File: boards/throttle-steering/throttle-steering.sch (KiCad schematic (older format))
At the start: 58 parts, among them IC1 ATMEGA16M1, P1 CONN_02X03, Q1 SSM3K333R, Q2 SSM3K333R, Q3 SSM3K333R, U1 MCP6021T-E/OT, U2 CAN_Transceiver, U3 MCP6021T-E/OT, U4 TPS561201, Y1 Crystal_SMD

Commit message: Updated the steering-throttle schematic. Need to check footprints and create netlist before going to layout.
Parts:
- removed R10, R16, R5: R_499, Resistors_SMD:R_0805, symbol R_499
- removed R13, R4: R_10k, Resistors_SMD:R_0805, symbol R_10k
- removed R14: R_200, Resistors_SMD:R_0805, symbol R_200
- removed R15, R8: R_100, Resistors_SMD:R_0805, symbol R_100
- removed R7: R, symbol R
- removed U1, U3: MCP6021T-E/OT, symbol MCP6021T-E/OT
- added D7: D_Zener_18V, footprints:DO-214AA, symbol D_Zener_18V
- added R10, R15, R16, R5, R7: R_1k, footprints:R_0805_OEM, symbol R_1k
- added R13, R4: R_1M, footprints:R_0805_OEM, symbol R_1M
- added R14, R8: R_2.2k, footprints:R_0805_OEM, symbol R_2.2k
- added U1, U3: MCP6001RT, footprints:SOT-23-5_OEM, symbol MCP6001RT
- gave numbers to parts that had none: 2
- renumbered D7 to D8, R23 to R22, R24 to R23, R27 to R24, R28 to R27, R29 to R28
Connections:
- wire segments 97 -> 79
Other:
- note removed: "50\n"
- moved on the sheet: J2

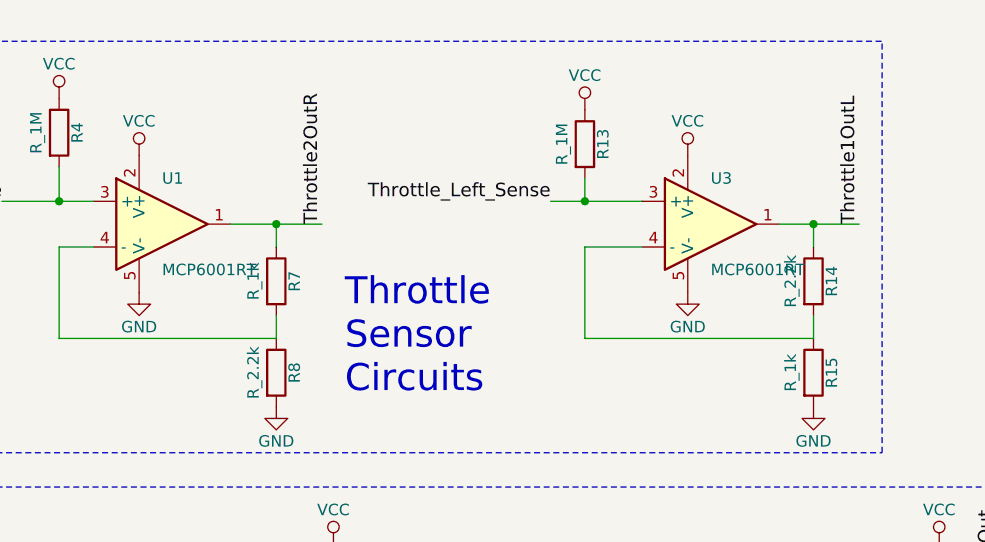
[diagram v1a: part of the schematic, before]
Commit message: Updated the throttle-steeting folder. Updated all of the footprints for the preset and began rough layout for board.
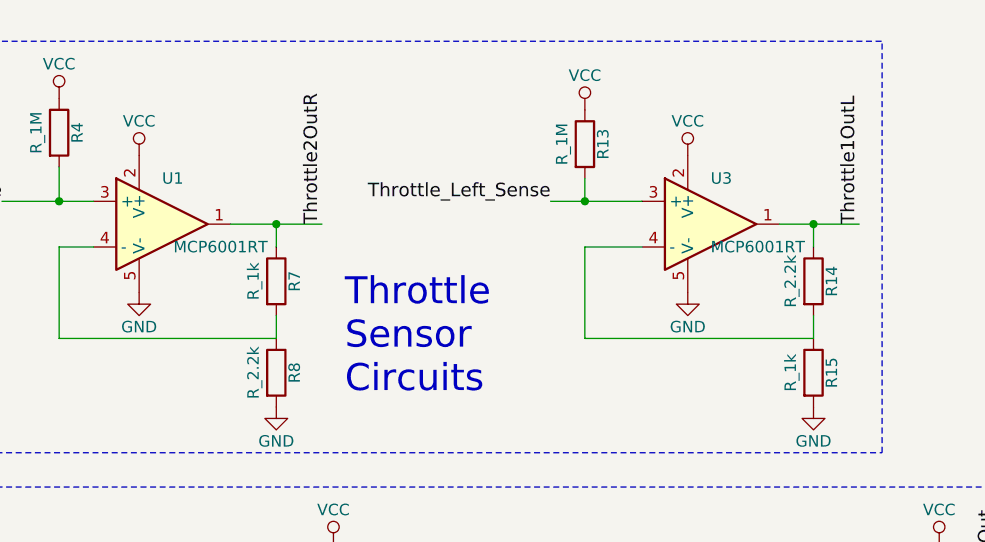
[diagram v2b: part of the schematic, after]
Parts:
- C1, C2, C3, C5, C6, C7, C8: footprint Capacitors_SMD:C_0805 -> footprints:C_0805_OEM
- C4: footprint Capacitors_SMD:C_1206 -> footprints:C_1206_OEM
- D1, D2, D3, D4, D5, D6: footprint LEDs:LED_0805 -> footprints:LED_0805_OEM
- D8, D9: footprint LEDs:LED_0805 -> footprints:D_0805_OEM
- Q1, Q2, Q3: footprint TO_SOT_Packages_SMD:SOT-23 -> footprints:SOT-23-5_OEM
- R1, R11, R12, R17, R18, R19, R2, R20, R21, R22, R23, R24, R25, R27, R28, R3, R6, R9: footprint Resistors_SMD:R_0805 -> footprints:R_0805_OEM
- R26: footprint Resistors_SMD:R_2512 -> footprints:R_2512_OEM
- U4: footprint TO_SOT_Packages_SMD:SOT-23-6 -> footprints:SOT-23-6_OEM

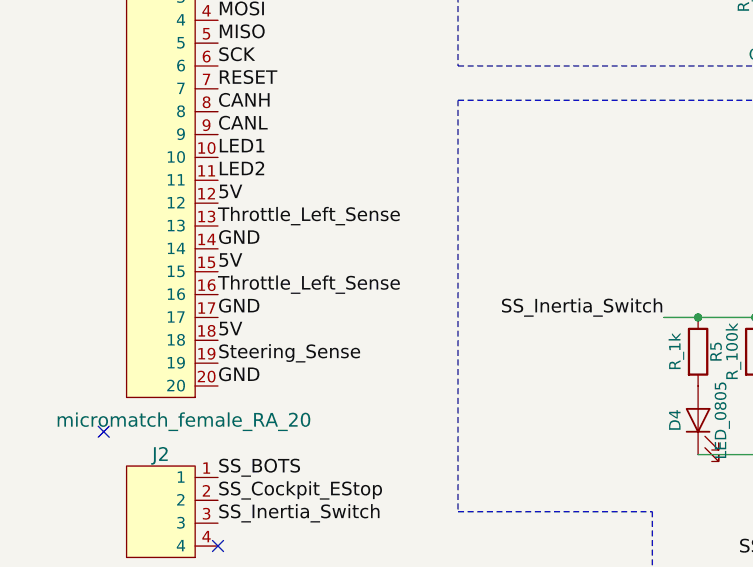
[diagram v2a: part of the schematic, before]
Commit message: Board is ready for layout.
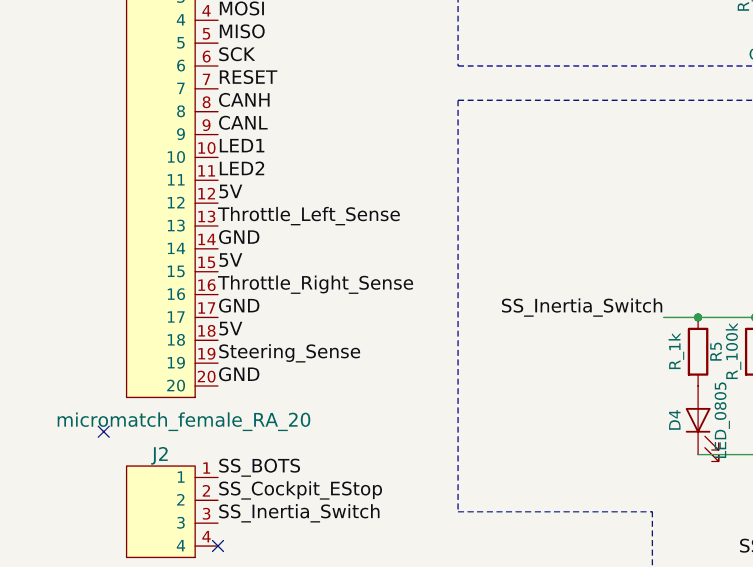
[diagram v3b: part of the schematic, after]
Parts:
- IC1: footprint Housings_QFP:TQFP-32_7x7mm_Pitch0.8mm -> footprints:TQFP-32_7x7mm_Pitch0.8mm
- U2: footprint Housings_SOIC:SOIC-8_3.9x4.9mm_Pitch1.27mm -> footprints:SOIC-8_3.9x4.9mm_Pitch1.27mm_OEM
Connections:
- net Throttle_Left_Sense: no longer J1.16
- net Throttle_Right_Sense: now also J1.16
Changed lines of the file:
@@
 F 0 "IC1" H 7650 4580 50  0000 L BNN
 F 1 "ATMEGA16M1" H 9100 1350 50  0000 L BNN
-F 2 "Housings_QFP:TQFP-32_7x7mm_Pitch0.8mm" H 8600 2750 50  0001 C CIN
+F 2 "footprints:TQFP-32_7x7mm_Pitch0.8mm" H 8600 2750 50  0001 C CIN
 F 3 "http://www.atmel.com/Images/Atmel-8209-8-bit%20AVR%20ATmega16M1-32M1-64M1_Datasheet.pdf" H 7650 4580 50  0001 C CNN
 F 4 "ATMEGA16M1-AU-ND" H 8600 2750 60  0001 C CNN "MPN"
@@
 F 0 "U2" H 4650 7400 50  0000 L CNN
 F 1 "CAN_Transceiver" H 5100 6700 50  0000 L CNN
-F 2 "Housings_SOIC:SOIC-8_3.9x4.9mm_Pitch1.27mm" H 5050 6550 50  0001 C CIN
+F 2 "footprints:SOIC-8_3.9x4.9mm_Pitch1.27mm_OEM" H 5050 6550 50  0001 C CIN
 F 3 "http://www.microchip.com/mymicrochip/filehandler.aspx?ddocname=en561044" H 4650 7400 50  0001 C CNN
 F 4 "Digi-Key" H 5050 7050 60  0001 C CNN "MFN"
@@
 5V
 Text Label 950  3450 0    59   ~ 0
-Throttle_Left_Sense
+Throttle_Right_Sense
 Text Label 950  3550 0    59   ~ 0
 GND

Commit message: Fixed wrong footprint.
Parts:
- Q1, Q2, Q3: footprint footprints:SOT-23-5_OEM -> footprints:SOT-23F
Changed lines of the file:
@@
 F 0 "Q3" H 6350 3625 50  0000 L CNN
 F 1 "SSM3K333R" H 6350 3550 50  0000 L CNN
-F 2 "footprints:SOT-23-5_OEM" H 6350 3475 50  0001 L CIN
+F 2 "footprints:SOT-23F" H 6350 3475 50  0001 L CIN
 F 3 "file:///home/sherrieshen/Downloads/SSM3K333R_datasheet_en_20140301.pdf" H 6350 3625 50  0001 L CNN
 F 4 "https://www.digikey.com/product-detail/en/toshiba-semiconductor-and-storage/SSM3K333RLF/SSM3K333RLFCT-ND/3522391" H 6450 3725 60  0001 C CNN "Purchase_Link"
@@
 F 0 "Q2" H 4750 4675 50  0000 L CNN
 F 1 "SSM3K333R" H 4750 4600 50  0000 L CNN
-F 2 "footprints:SOT-23-5_OEM" H 4750 4525 50  0001 L CIN
+F 2 "footprints:SOT-23F" H 4750 4525 50  0001 L CIN
 F 3 "file:///home/sherrieshen/Downloads/SSM3K333R_datasheet_en_20140301.pdf" H 4750 4675 50  0001 L CNN
 F 4 "https://www.digikey.com/product-detail/en/toshiba-semiconductor-and-storage/SSM3K333RLF/SSM3K333RLFCT-ND/3522391" H 4850 4775 60  0001 C CNN "Purchase_Link"
@@
 F 0 "Q1" H 3700 3625 50  0000 L CNN
 F 1 "SSM3K333R" H 3700 3550 50  0000 L CNN
-F 2 "footprints:SOT-23-5_OEM" H 3700 3475 50  0001 L CIN
+F 2 "footprints:SOT-23F" H 3700 3475 50  0001 L CIN
 F 3 "file:///home/sherrieshen/Downloads/SSM3K333R_datasheet_en_20140301.pdf" H 3700 3625 50  0001 L CNN
 F 4 "https://www.digikey.com/product-detail/en/toshiba-semiconductor-and-storage/SSM3K333RLF/SSM3K333RLFCT-ND/3522391" H 3800 3725 60  0001 C CNN "Purchase_Link"

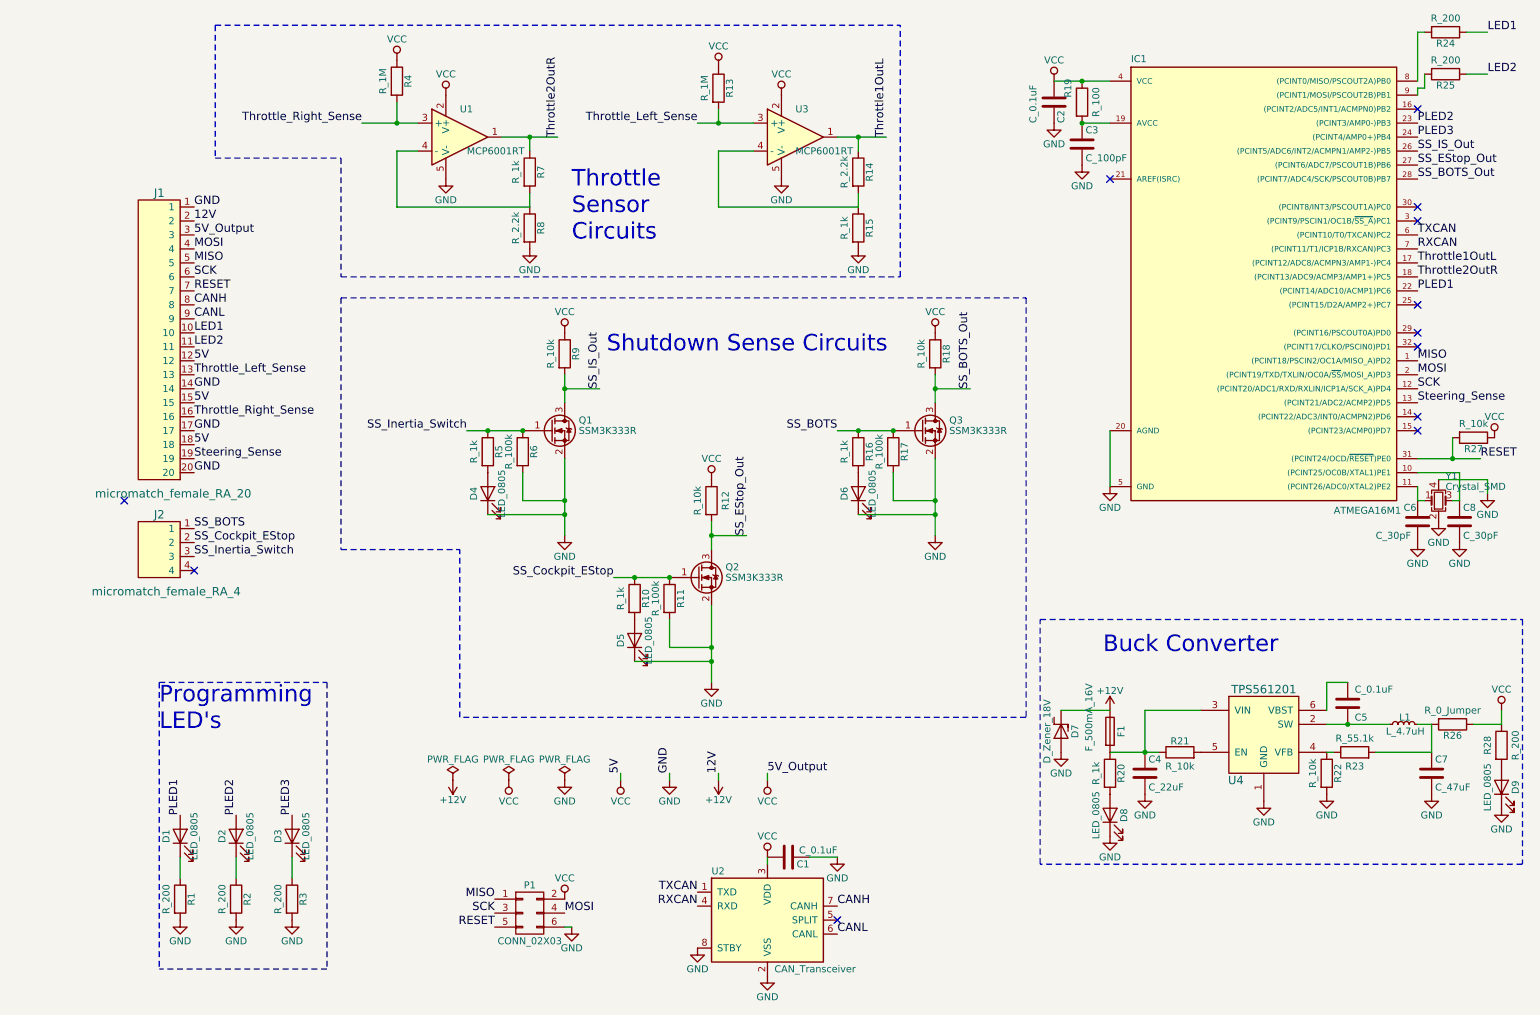
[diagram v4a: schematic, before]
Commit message: Updated schematic to include RTD-LD, as well as new dimensions for board
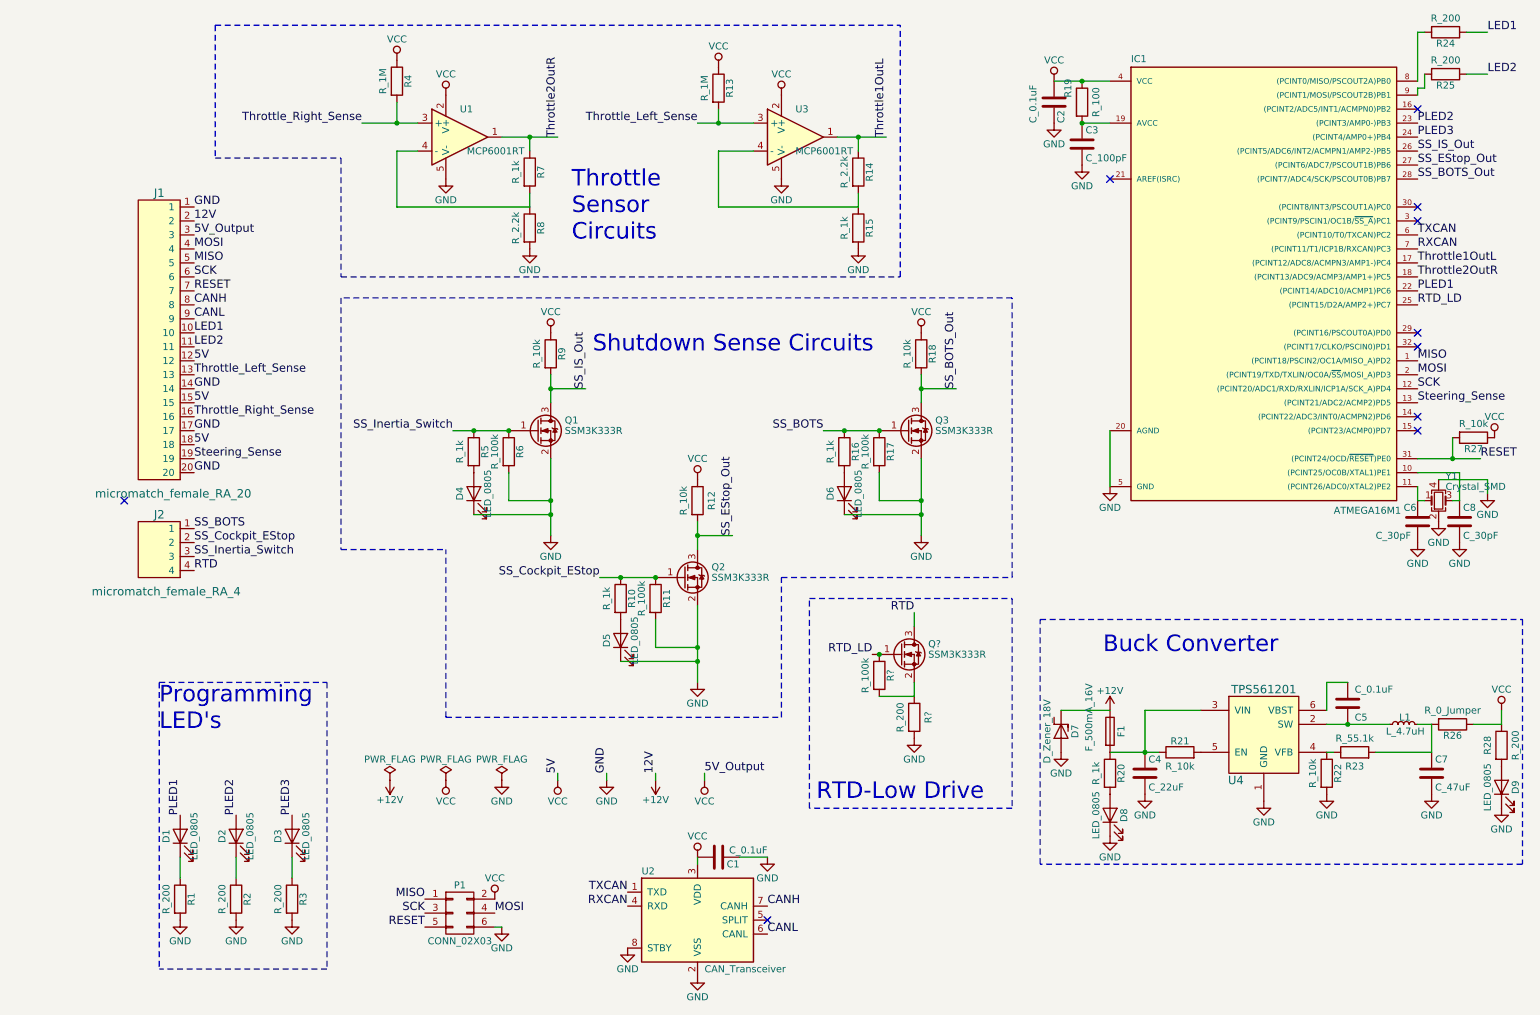
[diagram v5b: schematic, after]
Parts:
- added Q?: SSM3K333R, footprints:SOT-23F, symbol SSM3K333R
- added R?: R_200, Resistors_SMD:R_0805, symbol R_200
- added R?: R_100k, footprints:R_0805_OEM, symbol R_100k
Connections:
- net GND: now also R?.2
- net RTD_LD: now reaches IC1.25 ((PCINT15/D2A/AMP2+)PC7)
- net RTD_LD: now also Q?.1 (G)
- net RTD: now reaches J2.4
- net RTD: now also Q?.3 (D)
- new net: Q?.2 (S), R?.1, R?.2
- no-connect marks 12 -> 10
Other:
- note added: "RTD-Low Drive"
- moved on the sheet: C1, D4, D5, D6, P1, Q1, Q2, Q3, R10, R11, R12, R16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

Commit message: Final layout and tracing for throttle-steering
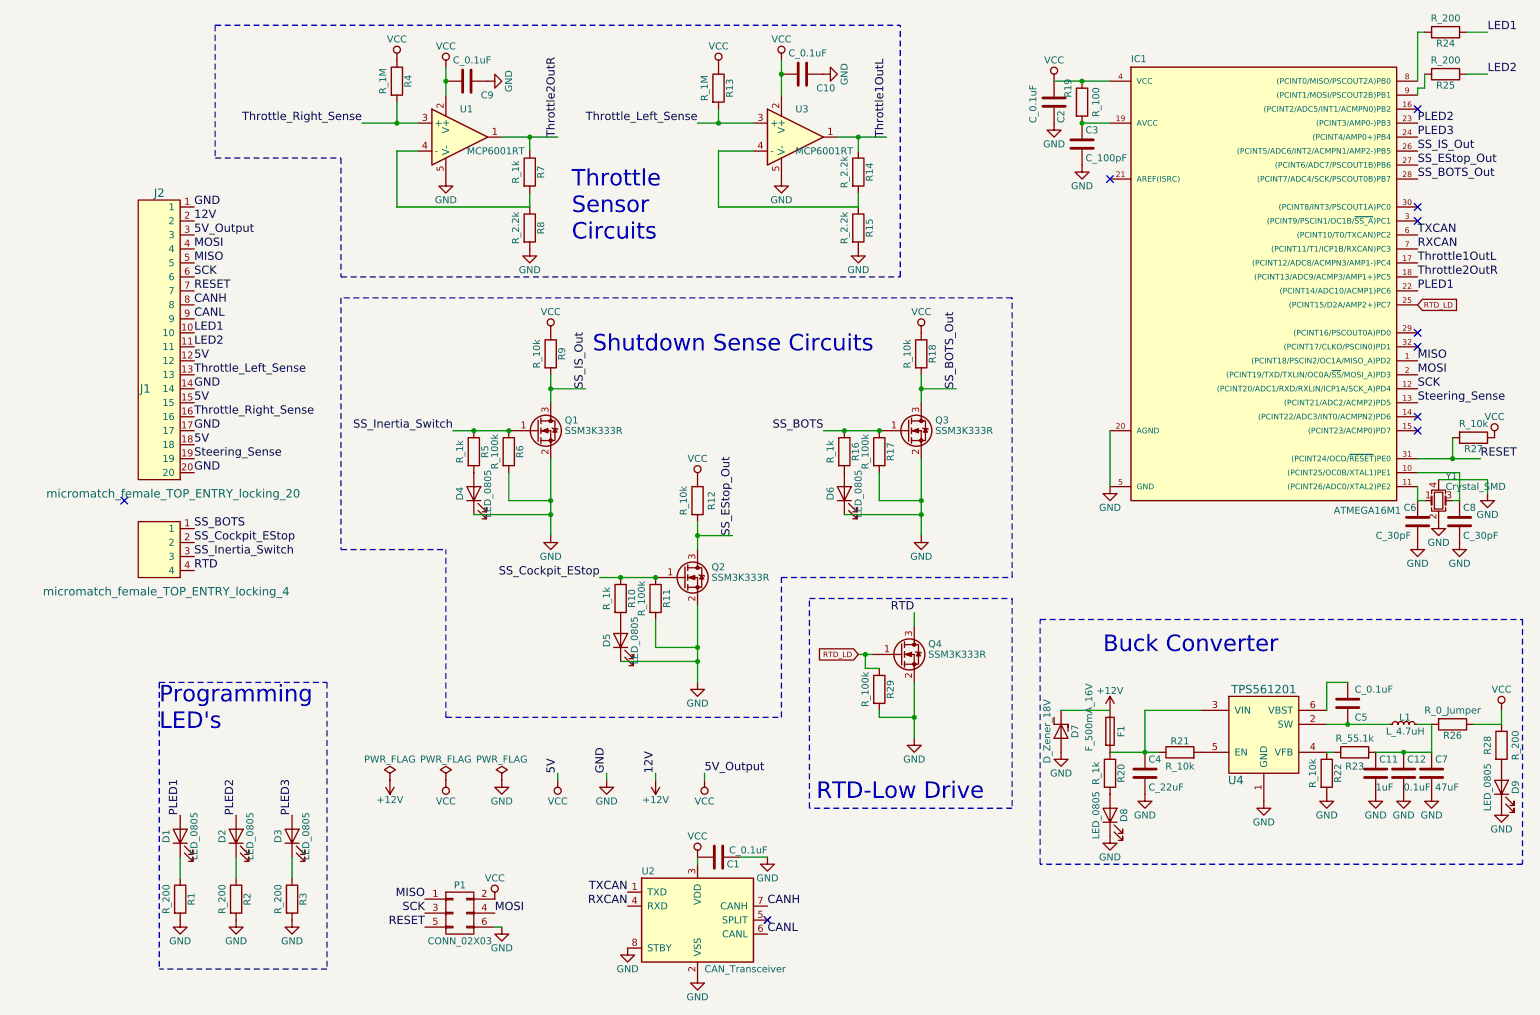
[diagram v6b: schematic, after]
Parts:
- removed J1: micromatch_female_RA_20, footprints:micromatch_female_ra_20, symbol micromatch_female_RA_20
- removed J2: micromatch_female_RA_4, footprints:micromatch_female_ra_4, symbol micromatch_female_RA_4
- removed R15: R_1k, footprints:R_0805_OEM, symbol R_1k
- removed R?: R_200, Resistors_SMD:R_0805, symbol R_200
- removed R?: R_100k, footprints:R_0805_OEM, symbol R_100k
- added C10, C9: C_0.1uF, footprints:C_0805_OEM, symbol C_0.1uF
- added C11: 1uF, footprints:C_0805_OEM, symbol C_1uF
- added C12: 0.1uF, footprints:C_0805_OEM, symbol C_0.1uF
- added J1: micromatch_female_TOP_ENTRY_locking_4, footprints:micromatch_female_vert_4, symbol micromatch_female_TOP_ENTRY_locking_4
- added J2: micromatch_female_TOP_ENTRY_locking_20, footprints:micromatch_female_vert_20, symbol micromatch_female_TOP_ENTRY_locking_20
- added R15: R_2.2k, footprints:R_0805_OEM, symbol R_2.2k
- added R29: R_100k, footprints:R_0805_OEM, symbol R_100k
- C7: value C_47uF -> 47uF
- gave numbers to parts that had none: 1
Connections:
- net +12V: now also J2.2
- net CANH: now also J2.8
- net CANL: now also J2.9
- net GND: now also Q4.2 (S), C10.1, C11.2, C12.2, C9.1, J2.1, J2.14, J2.17, J2.20, R15.2, R29.2
- net LED1: now also J2.10
- net LED2: now also J2.11
- net MISO: now also J2.5
- net MOSI: now also J2.4
- net RESET: now also J2.7
- net RTD: now also J1.4
- net RTD_LD: now also R29.1
- net SCK: now also J2.6
- net SS_BOTS: now also J1.1
- net SS_Cockpit_EStop: now also J1.2
- net SS_Inertia_Switch: now also J1.3
- net Steering_Sense: now also J2.19
- net Throttle_Left_Sense: now also J2.13
- net Throttle_Right_Sense: now also J2.16
- net VCC: now also C10.2, C9.2, J2.12, J2.15, J2.18, J2.3
- net at C7.1, L1.2, R23.2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: now also C11.1, C12.1
- net at R14.2, U3.4 (-): now also R15.1
